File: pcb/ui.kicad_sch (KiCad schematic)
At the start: 9 parts, among them Q1 2N7002, Q13 BSS84, Q14 BSS84, Q15 BSS84, Q16 BSS84, U18 NHD-C12864A1Z-FSW-FBW-HTT, U23 74LVC1G139, U24 TLC5927IPWPR

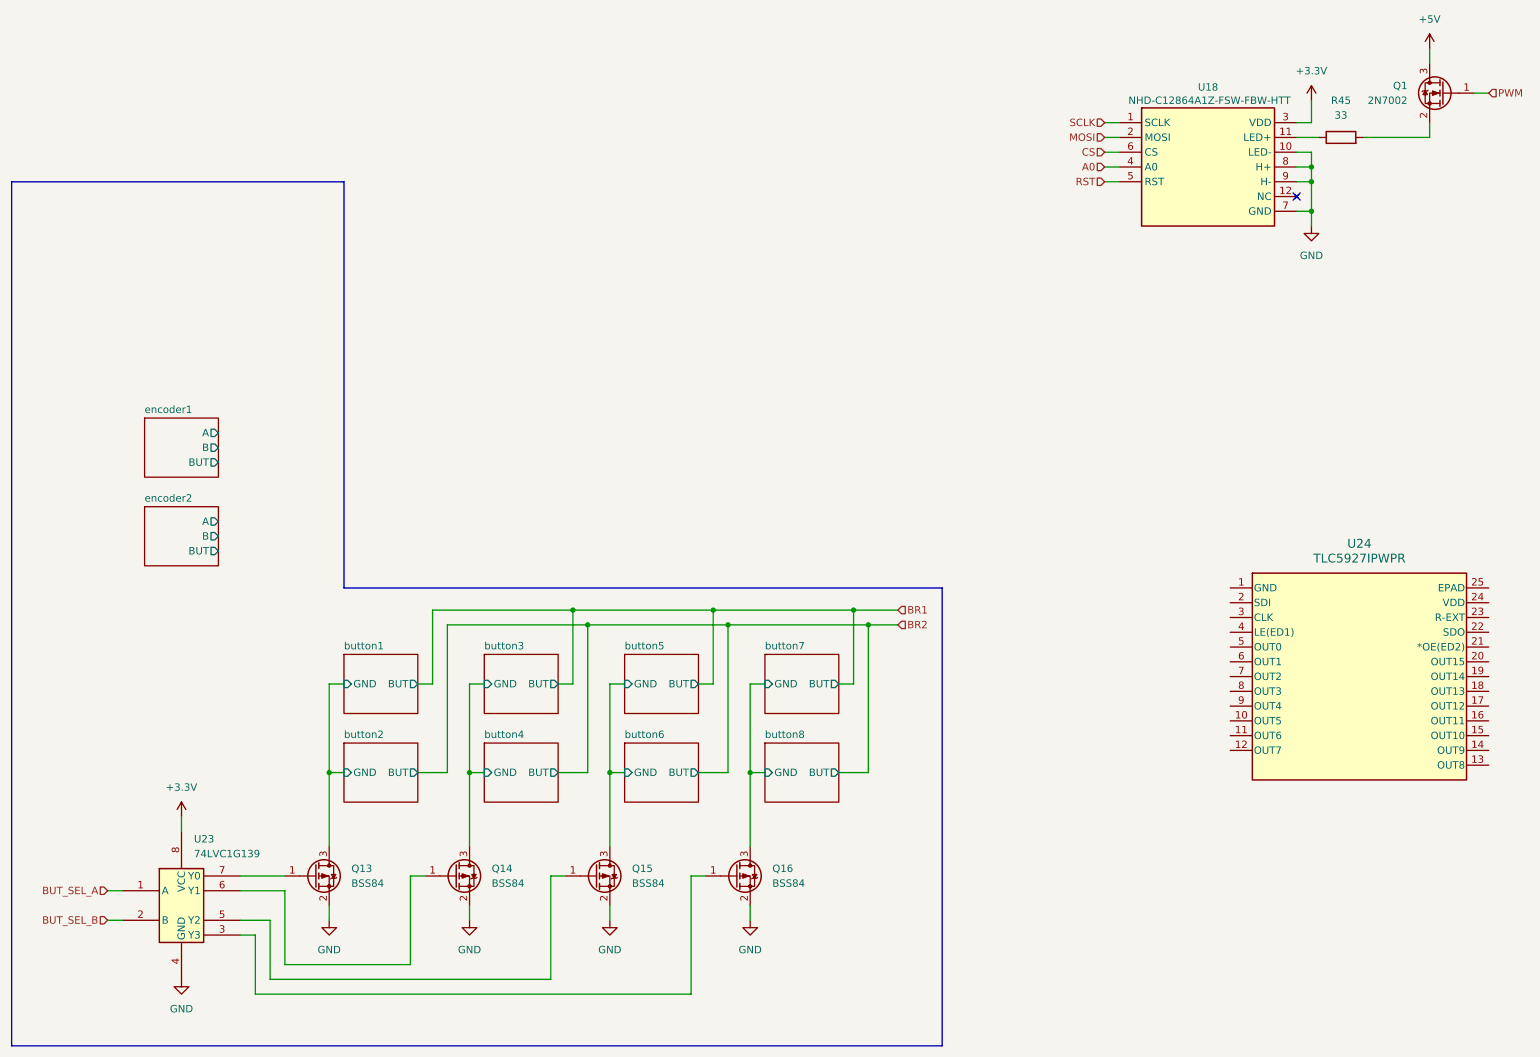
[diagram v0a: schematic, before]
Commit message: rework to tia feedback selection, board power, and ui
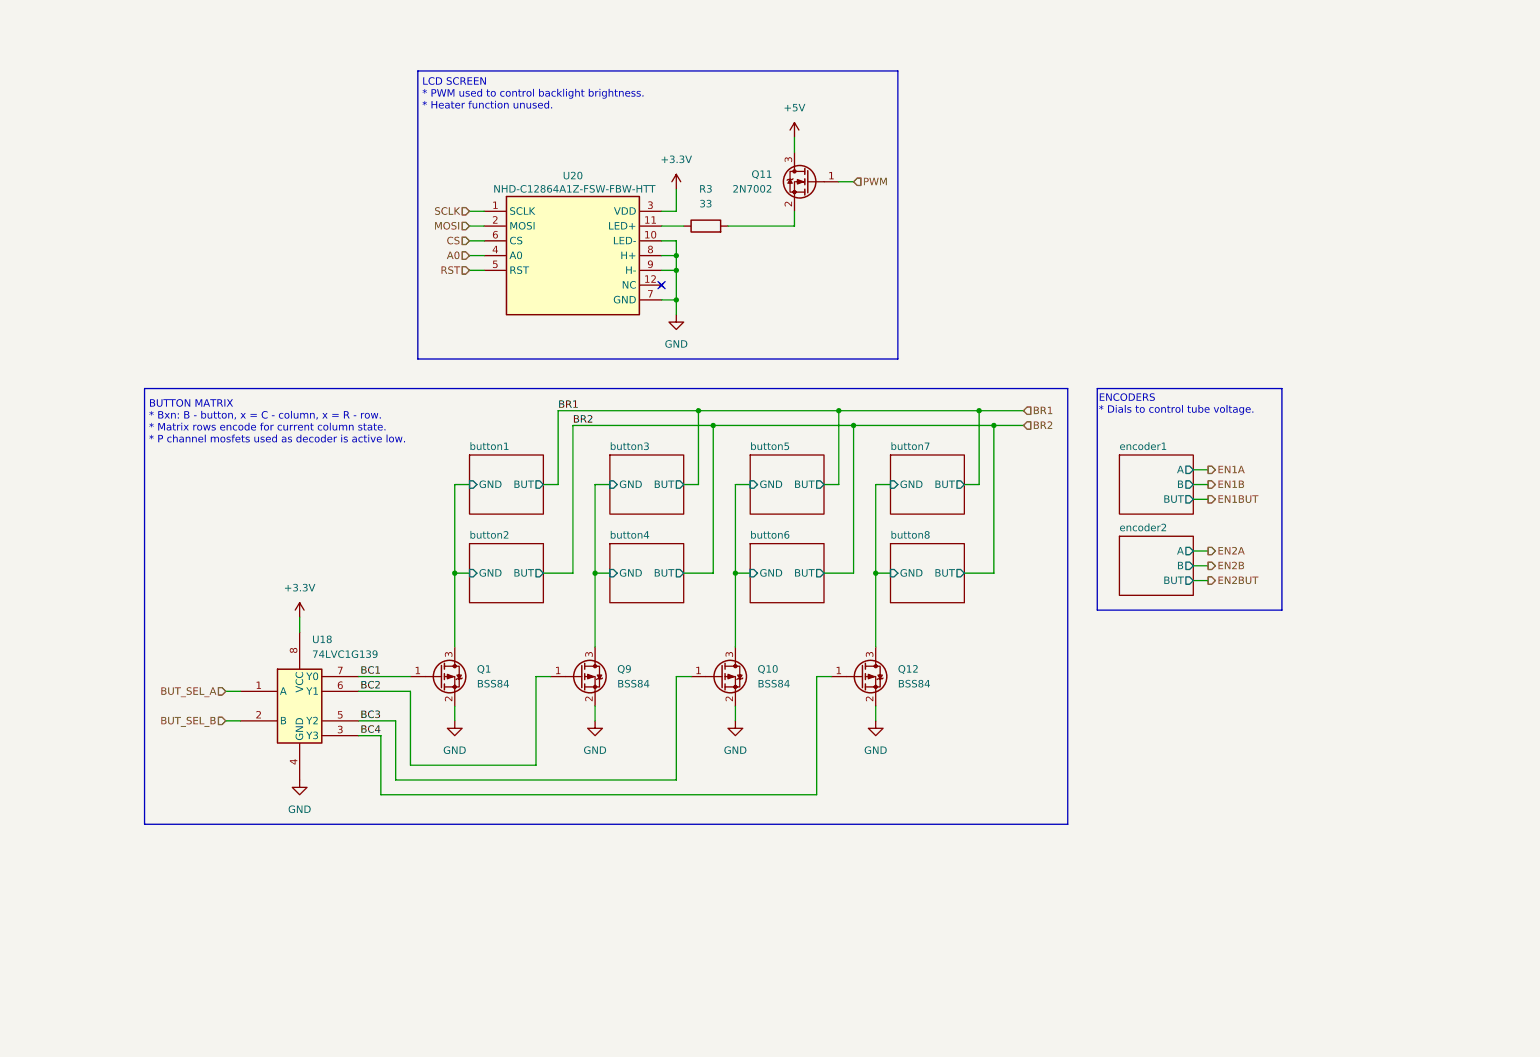
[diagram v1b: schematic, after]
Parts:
- removed U24: TLC5927IPWPR, PWP24_4P87X2P4, symbol project_library:TLC5927IPWPR
- renumbered Q13 to Q1, Q15 to Q10, Q1 to Q11, Q16 to Q12, Q14 to Q9, R45 to R3, U23 to U18, U18 to U20
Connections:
- net BC2: now reaches Q9.1 (G), U18.6 (Y1)
- net BC3: now reaches Q10.1 (G), U18.5 (Y2)
- net BC4: now reaches Q12.1 (G), U18.3 (Y3)
- net BC1: now reaches Q1.1 (G), U18.7 (Y0)
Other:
- note added: "BUTTON MATRIX * Bxn: B - button, x = C - column, x = R - row. * Matrix rows encode for current column state. * P channel mosfets used as decoder is active low."
- note added: "ENCODERS * Dials to control tube voltage."
- note added: "LCD SCREEN * PWM used to control backlight brightness. * Heater function unused."
- moved on the sheet: Q1, Q10, Q11, Q12, Q9, R3, U18, U20
